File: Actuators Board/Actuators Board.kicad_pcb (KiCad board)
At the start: 2 copper layers, 50 x 50 mm, 113 parts, among them IC1 BD62120AEFJ-E2, J1 Conn_01x05_Male, J10 Conn_01x02_Male, J2 Solenoid(Sol), J3 USB_C_Receptacle_USB2.0, J4 Conn_01x03_Male, J5 Conn_01x06_Male, J9 Conn_01x02_Male, Q1 MMDT2222A, Q2 SI2366DS, U1 ESP32-PICO-D4, U2 TPS54233D, U3 CP2102-GMR-QFN28, U4 SN65HVD230, U5 LTC4411, U6 RT9025-25GSP, U7 LTC4411

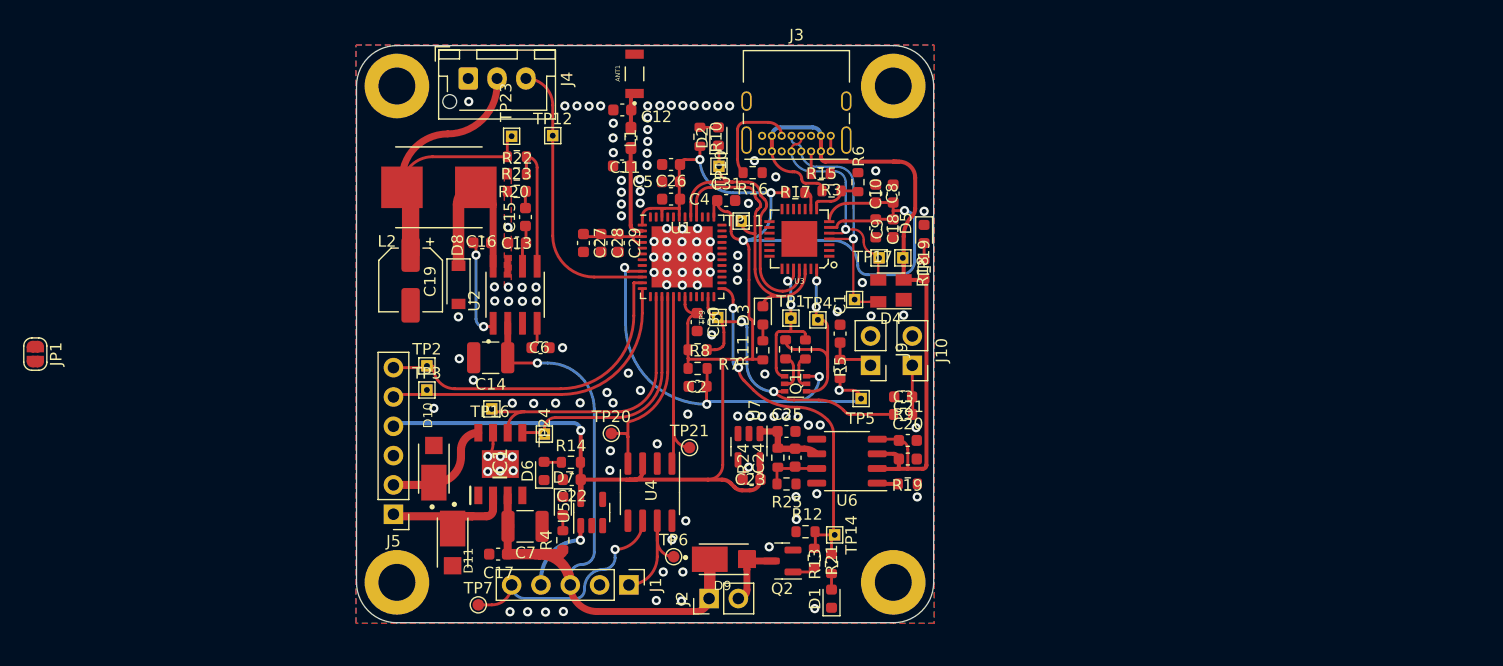
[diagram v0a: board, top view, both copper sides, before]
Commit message: Swapped RBUS connector, layout needs update.
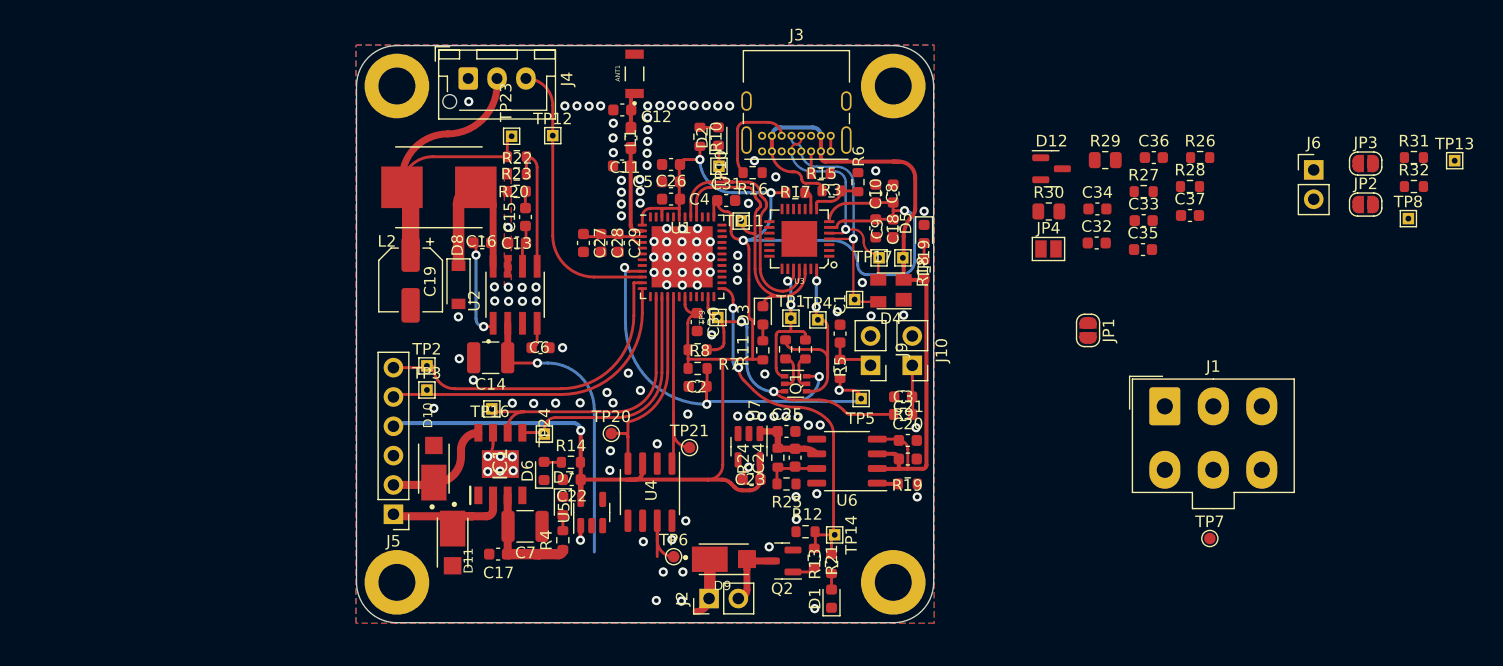
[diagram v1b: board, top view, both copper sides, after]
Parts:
- added C32: 160pF, Capacitor_SMD:C_0603_1608Metric, F.Cu at (119.1, 47.1)
- added C33: 100nF, Capacitor_SMD:C_0603_1608Metric, F.Cu at (123.2, 45.2)
- added C34: 10uF, Capacitor_SMD:C_0603_1608Metric, F.Cu at (119.2, 44.1)
- added C35: 0.1uF, Capacitor_SMD:C_0603_1608Metric, F.Cu at (123.1, 47.7)
- added C36: 220pF, Capacitor_SMD:C_0603_1608Metric, F.Cu at (124.1, 39.7)
- added C37: 220 pF, Capacitor_SMD:C_0603_1608Metric, F.Cu at (127.2, 44.7)
- added D12: SM712_SOT23, Package_TO_SOT_SMD:SOT-23, F.Cu at (115.2, 40.7)
- added J6: Conn_01x02_Female, Connector_PinHeader_2.54mm:PinHeader_1x02_P2.54mm_Vertical, F.Cu at (137.9, 40.8)
- added JP2: Pull-Down, Jumper:SolderJumper-2_P1.3mm_Open_RoundedPad1.0x1.5mm, F.Cu at (142.4, 43.8)
- added JP3: Pull-Up, Jumper:SolderJumper-2_P1.3mm_Open_RoundedPad1.0x1.5mm, F.Cu at (142.4, 40.2)
- added JP4: SolderJumper_2_Open, Jumper:SolderJumper-2_P1.3mm_Open_Pad1.0x1.5mm, F.Cu at (114.9, 47.6)
- added R26: 90, Resistor_SMD:R_0603_1608Metric, F.Cu at (128.1, 39.7)
- added R27: 90, Resistor_SMD:R_0603_1608Metric, F.Cu at (123.2, 42.6)
- added R28: 10k, Resistor_SMD:R_0603_1608Metric, F.Cu at (127.2, 42.2)
- added R29: 60, Resistor_SMD:R_0805_2012Metric, F.Cu at (119.9, 39.9)
- added R30: 60, Resistor_SMD:R_0805_2012Metric, F.Cu at (115.0, 44.4)
- added R31: 10k, Resistor_SMD:R_0603_1608Metric, F.Cu at (146.6, 39.7)
- added R32: 10k, Resistor_SMD:R_0603_1608Metric, F.Cu at (146.6, 42.2)
- added TP13: TestPoint, TestPoint:TestPoint_THTPad_1.0x1.0mm_Drill0.5mm, F.Cu at (150.1, 40.0)
- added TP8: TestPoint, TestPoint:TestPoint_THTPad_1.0x1.0mm_Drill0.5mm, F.Cu at (146.1, 45.0)
- J1: footprint Connector_PinHeader_2.54mm:PinHeader_1x05_P2.54mm_Vertical -> Connector_Molex:Molex_Mini-Fit_Jr_5566-06A_2x03_P4.20mm_Vertical
- moved JP1 91.2 mm to (118.4, 54.7)
- moved TP7 63.6 mm to (128.9, 72.7)
- moved J1 48.9 mm to (125.0, 61.2), turned to 0 degrees
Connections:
- J1 pad 1: /CAN_HIGH -> GND
- J1 pad 3: +24V -> Net-(U5-Pad1)
- J1 pad 4: Net-(J1-Pad4) -> +24V
- J1 pad 5: /CAN_LOW -> /CAN_HIGH
- U1 pad 27: unconnected-(U1-Pad27) -> /SSRGPIO
- U4 pad 1: /CAN_TX -> Net-(C32-Pad2)
- U4 pad 4: /CAN_RX -> Net-(R27-Pad2)
- U4 pad 5: unconnected-(U4-Pad5) -> /CAN-BUS/Vref
- U4 pad 8: GND -> Net-(R28-Pad1)
- U5 pad 1: Net-(J1-Pad4) -> Net-(U5-Pad1)
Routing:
- net +24V: track 63.6 -> 42.7 mm
- net /CAN_LOW: track 19.8 -> 0.11 mm
- net Net-(J1-Pad4): track 6.97 -> 0.00 mm, vias 1 -> 0
- net /CAN_HIGH: track 10.7 -> 6.98 mm
- net Net-(U5-Pad1): track 0.00 -> 1.28 mm, vias 0 -> 1
- net GND: vias 121 -> 117

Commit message: Added CAN transceiver and new connector to board
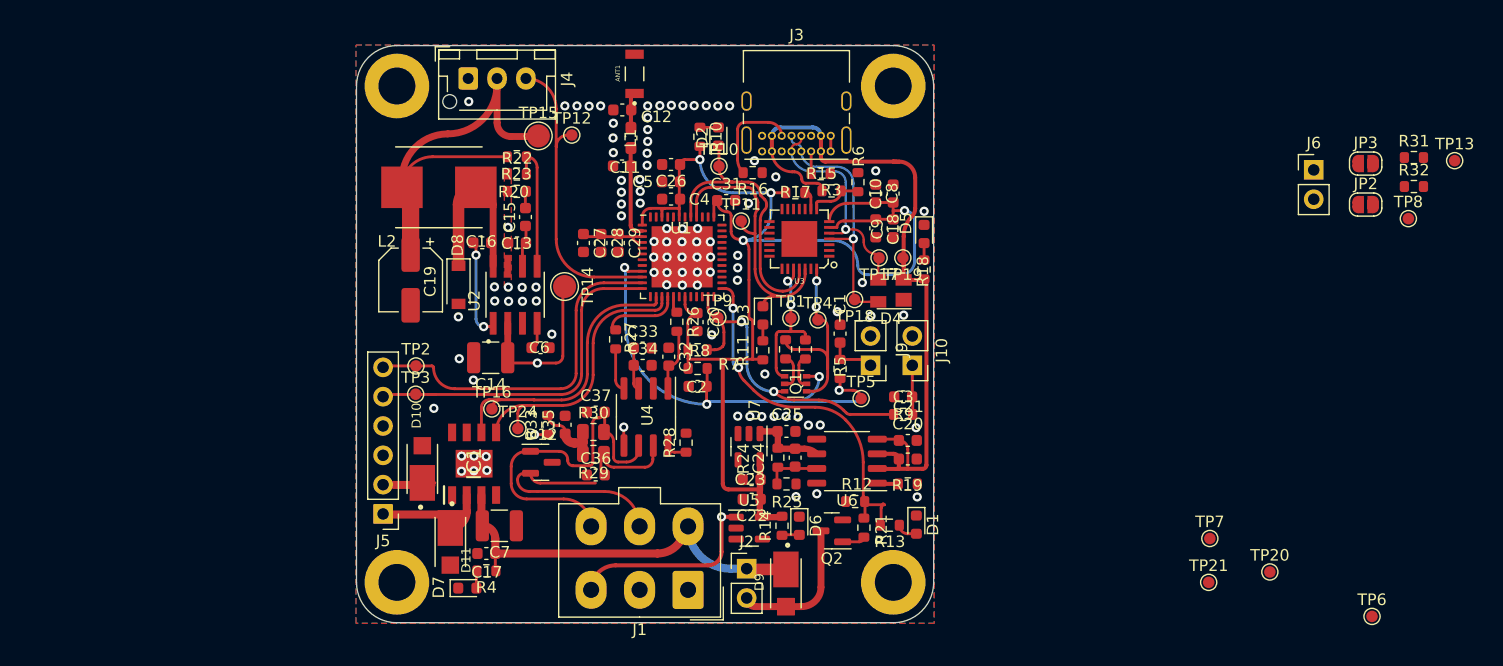
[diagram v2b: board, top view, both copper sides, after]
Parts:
- removed JP1: SolderJumper_2_Open, Jumper:SolderJumper-2_P1.3mm_Open_RoundedPad1.0x1.5mm
- removed JP4: SolderJumper_2_Open, Jumper:SolderJumper-2_P1.3mm_Open_Pad1.0x1.5mm
- removed TP23: TestPoint, TestPoint:TestPoint_THTPad_1.0x1.0mm_Drill0.5mm
- added R33: 0, Resistor_SMD:R_0603_1608Metric, F.Cu at (71.6, 62.9)
- added TP15: TestPoint, TestPoint:TestPoint_Pad_D2.0mm, F.Cu at (70.8, 37.8)
- TP1, TP10, TP11, TP12, TP13, TP16, TP17, TP18, TP19, TP2, TP24, TP3, TP4, TP5, TP8, TP9: footprint TestPoint:TestPoint_THTPad_1.0x1.0mm_Drill0.5mm -> TestPoint:TestPoint_Pad_D1.0mm
- TP14: footprint TestPoint:TestPoint_THTPad_1.0x1.0mm_Drill0.5mm -> TestPoint:TestPoint_Pad_D2.0mm
- moved TP6 60.7 mm to (143.0, 79.5)
- moved TP20 58.3 mm to (134.1, 75.6)
- moved C36 55.6 mm to (75.7, 67.2)
- moved C37 54.2 mm to (75.7, 61.8)
- moved C35 52.3 mm to (73.1, 62.9), turned to 90 degrees
- moved R29 51.1 mm to (75.5, 65.4), turned to 180 degrees
- moved D12 51.0 mm to (71.0, 66.1)
- moved R28 49.0 mm to (83.5, 64.4), turned to 90 degrees
- moved R26 47.5 mm to (82.8, 53.9), turned to -90 degrees
- moved R27 47.5 mm to (77.5, 55.5), turned to -90 degrees
- moved TP21 46.5 mm to (128.8, 76.5)
- moved C33 44.8 mm to (79.8, 56.2)
- moved J1 44.3 mm to (83.7, 77.2), turned to 180 degrees
- moved R30 43.8 mm to (75.5, 63.5)
- moved C34 41.7 mm to (79.8, 57.7)
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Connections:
- D12 pad 1: /CAN_HIGH -> /CAN_LOW
- D12 pad 2: /CAN_LOW -> /CAN_HIGH
- TP14 pad 1: /SolEN -> +24V
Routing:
- net /CAN_LOW: track 0.11 -> 32.5 mm, vias 1 -> 0
- net +3V3: track 154.6 -> 124.1 mm, vias 5 -> 4
- net /CAN_HIGH: track 6.98 -> 29.1 mm
- net /CAN_TX: track 18.4 -> 1.50 mm
- net Net-(J1-Pad3): track 1.28 -> 17.3 mm
- net /CAN_RX: track 17.6 -> 6.90 mm
- net +24V: track 42.7 -> 50.8 mm
- net Net-(C35-Pad1): track 0.00 -> 6.77 mm
- net /Motor-: track 10.6 -> 4.43 mm
- net +6V: track 32.5 -> 38.6 mm
- net /SolGND: track 6.60 -> 12.6 mm
- net Net-(C32-Pad2): track 0.00 -> 5.63 mm
- net Net-(R27-Pad2): track 0.00 -> 3.81 mm
- net GND: track 5.11 -> 1.72 mm, vias 117 -> 95
- net /CAN-BUS/Vref: track 0.00 -> 2.77 mm, vias 0 -> 2
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
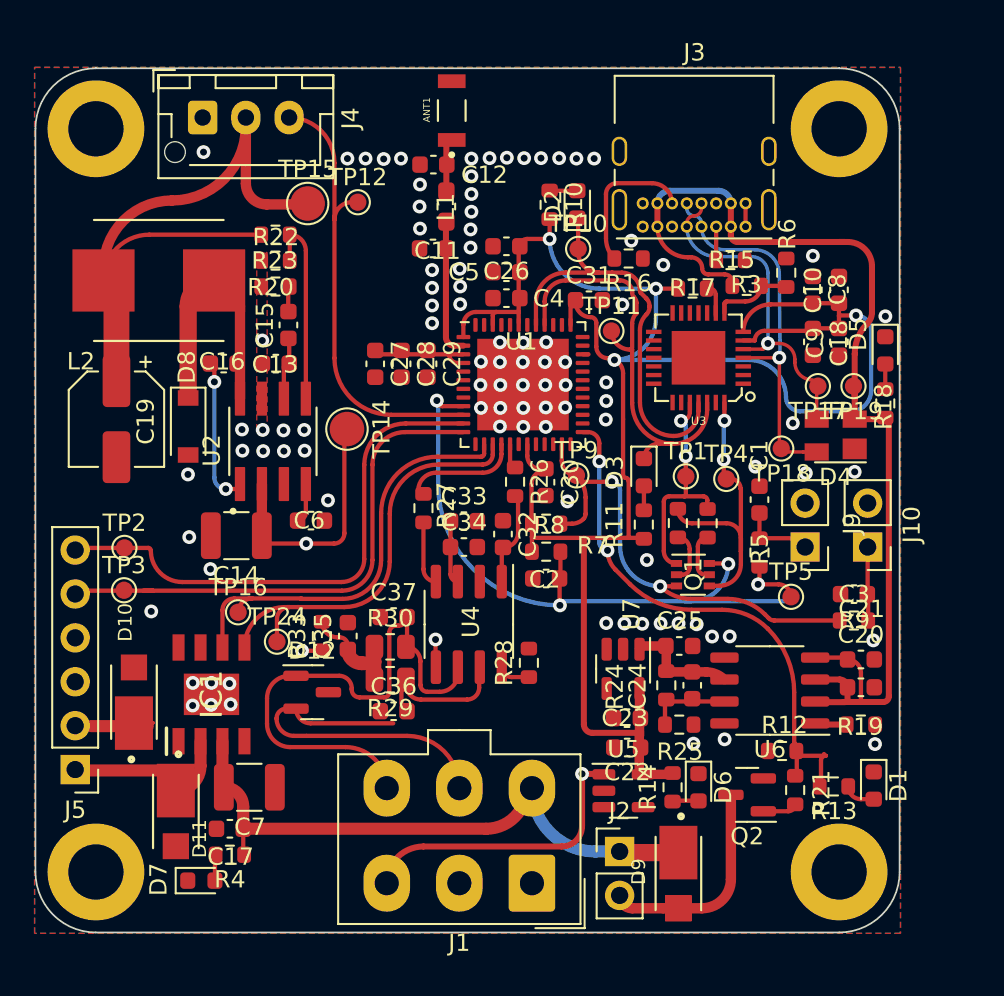
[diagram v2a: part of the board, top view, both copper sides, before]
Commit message: Converted pcb into 4 layers and fixed schematic merge issues
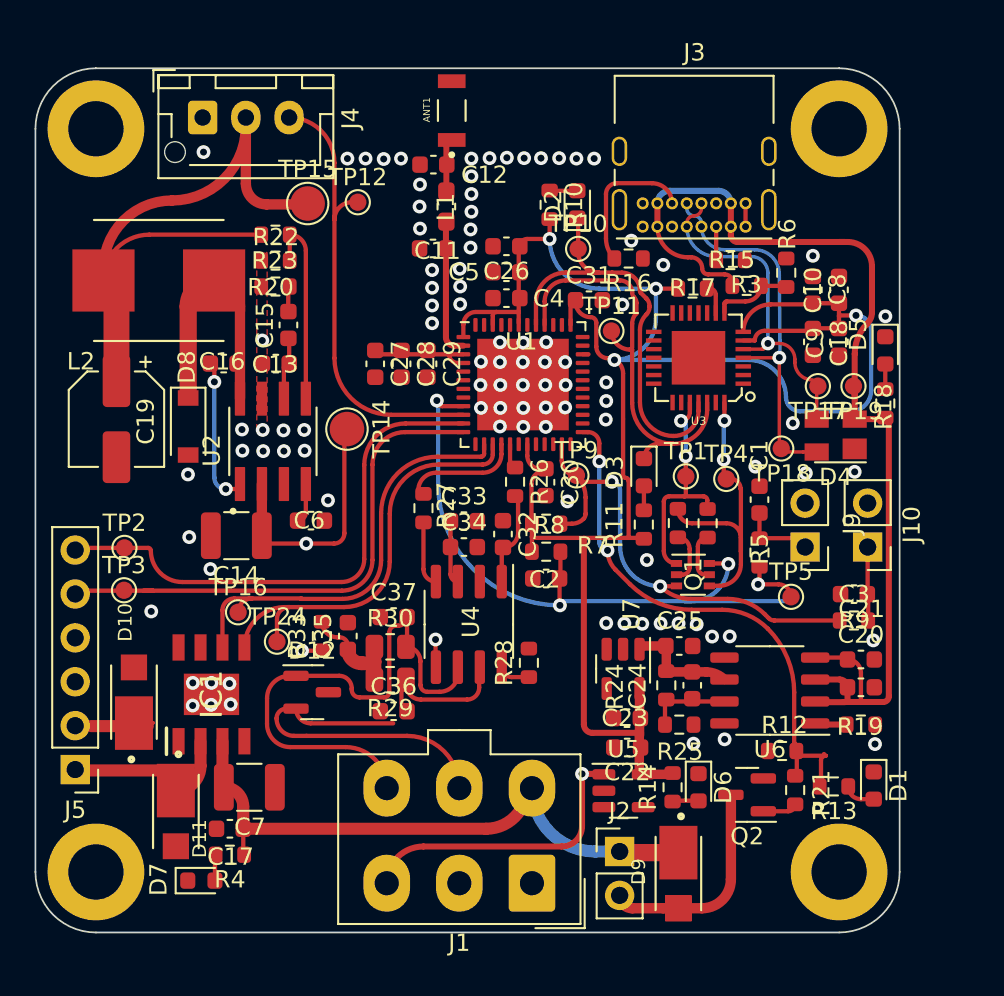
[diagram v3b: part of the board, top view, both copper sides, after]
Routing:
- added copper zone on In2.Cu, net +3V3
- added copper zone on In1.Cu, net GND
- removed copper zone on B.Cu, net GND
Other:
- copper layers 2 -> 4
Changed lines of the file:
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@@
 (kicad_pcb (version 20211014) (generator pcbnew)
   (general
-    (thickness 1.6)
+    (thickness 1.599998)
   )
   (paper "A4")
   (layers
     (0 "F.Cu" jumper)
+    (1 "In1.Cu" signal)
+    (2 "In2.Cu" signal)
     (31 "B.Cu" signal)
     (32 "B.Adhes" user "B.Adhesive")
@@
       (layer "F.Mask" (type "Top Solder Mask") (thickness 0.01))
       (layer "F.Cu" (type "copper") (thickness 0.035))
-      (layer "dielectric 1" (type "core") (thickness 1.51) (material "FR4") (epsilon_r 4.5) (loss_tangent 0.02))
+      (layer "dielectric 1" (type "prepreg") (thickness 0.491666) (material "FR4") (epsilon_r 4.5) (loss_tangent 0.02))
+      (layer "In1.Cu" (type "copper") (thickness 0.0175))
+      (layer "dielectric 2" (type "core") (thickness 0.491666) (material "FR4") (epsilon_r 4.5) (loss_tangent 0.02))
+      (layer "In2.Cu" (type "copper") (thickness 0.0175))
+      (layer "dielectric 3" (type "prepreg") (thickness 0.491666) (material "FR4") (epsilon_r 4.5) (loss_tangent 0.02))
       (layer "B.Cu" (type "copper") (thickness 0.035))
       (layer "B.Mask" (type "Bottom Solder Mask") (thickness 0.01))
@@
     (fp_line (start -1.62 2.4) (end -1.62 3.3) (layer "F.SilkS") (width 0.12))
     (fp_line (start 7.57 2.4) (end 7.57 3.3) (layer "F.SilkS") (width 0.12))
-    (fp_line (start -2.3 -1.06) (end -2.3 9.11) (layer "F.CrtYd") (width 0.05))
     (fp_line (start -2.3 9.11) (end 8.25 9.11) (layer "F.CrtYd") (width 0.05))
+    (fp_line (start -2.3 -1.06) (end -2.3 9.11) (layer "F.CrtYd") (width 0.05))
     (fp_line (start 8.25 -1.06) (end 8.25 9.11) (layer "F.CrtYd") (width 0.05))
     (fp_line (start -2.3 -1.06) (end 8.25 -1.06) (layer "F.CrtYd") (width 0.05))
@@
   )
   (zone (net 2) (net_name "GND") (layer "F.Cu") (hatch edge 0.508)
-    (connect_pads (clearance 0.254))
+    (connect_pads (clearance 0))
     (min_thickness 0.254) (filled_areas_thickness no)
     (fill (thermal_gap 0.508) (thermal_bridge_width 0.508))
     (polygon
       (pts
-        (xy 105.05 80.05)
-        (xy 54.95 80.05)
-        (xy 54.95 29.95)
-        (xy 105.05 29.95)
+        (xy 68.404338 50.929497)
+        (xy 67.805026 50.929498)
+        (xy 67.80501 40.652611)
+        (xy 68.404322 40.65261)
       )
     )
   )
-  (zone (net 2) (net_name "GND") (layer "F.Cu") (hatch edge 0.508)
-    (connect_pads (clearance 0))
+  (zone (net 2) (net_name "GND") (layer "In1.Cu") (hatch edge 0.508)
+    (connect_pads (clearance 0.254))
     (min_thickness 0.254) (filled_areas_thickness no)
-    (fill (thermal_gap 0.508) (thermal_bridge_width 0.508))
+    (fill yes (thermal_gap 0.508) (thermal_bridge_width 0.508))
     (polygon
       (pts
-        (xy 68.404338 50.929497)
-        (xy 67.805026 50.929498)
-        (xy 67.80501 40.652611)
-        (xy 68.404322 40.65261)
+        (xy 105.05 80.05)
+        (xy 54.95 80.05)
+        (xy 54.95 29.95)
+        (xy 105.05 29.95)
       )
     )
   )
-  (zone (net 2) (net_name "GND") (layer "B.Cu") (hatch edge 0.508)
+  (zone (net 5) (net_name "+3V3") (layer "In2.Cu") (hatch edge 0.508)
     (connect_pads (clearance 0.508))
     (min_thickness 0.254) (filled_areas_thickness no)
-    (fill (thermal_gap 0.508) (thermal_bridge_width 0.508))
+    (fill yes (thermal_gap 0.508) (thermal_bridge_width 0.508))
     (polygon
       (pts
